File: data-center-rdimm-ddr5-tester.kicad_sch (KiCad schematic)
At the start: 2 parts

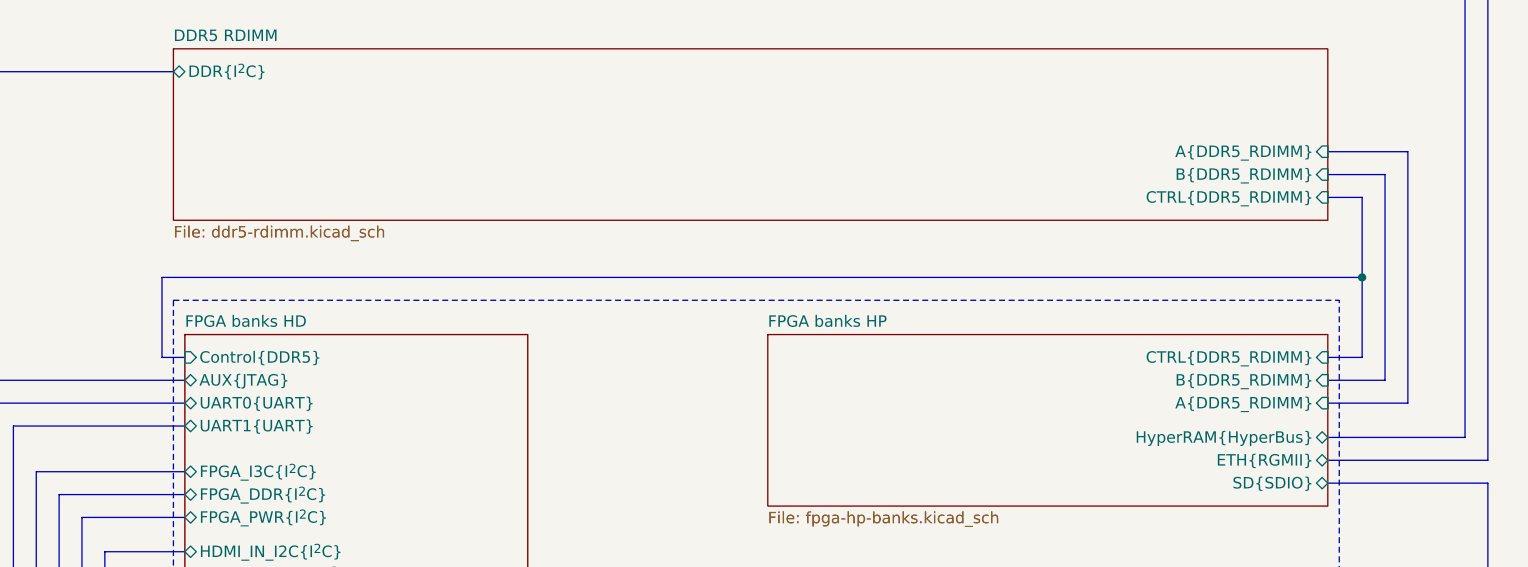
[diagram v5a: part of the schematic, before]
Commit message: [#68016] Solve ERC warrings and errors
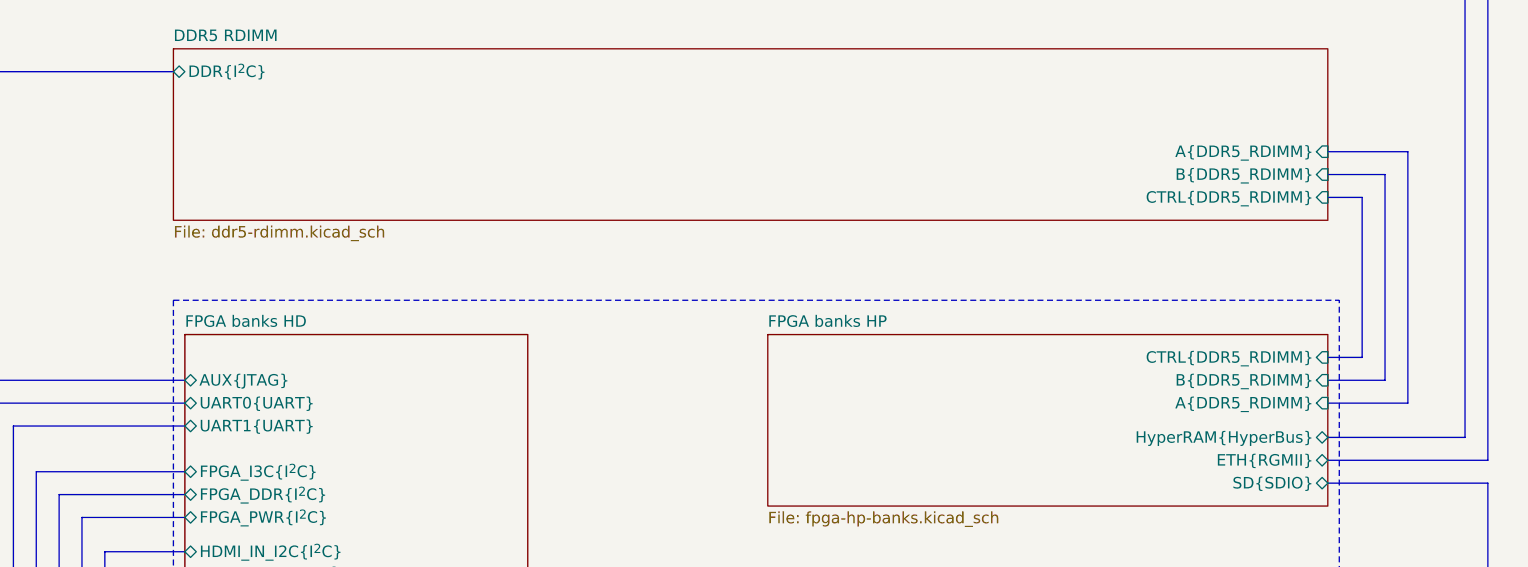
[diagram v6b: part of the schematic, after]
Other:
- sheet FPGA banks HD ports: added none; removed Control{DDR5}
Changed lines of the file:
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@@
     (comment 2 "Antmicro Ltd")
   )
-  (bus_alias "DDR5_RDIMM" (members "DQ[0..31]" "CA[0..6]" "CB[0..7]" "CK_P" "CK_N" "PAR" "DLBDQ" "DLBDQS" "~{ALERT}" "~{RESET}" "DQS0_P" "DQS0_N" "DQS1_P" "DQS1_N" "DQS2_P" "DQS2_N" "DQS3_P" "DQS3_N" "DQS4_P" "DQS4_N" "DQS5_P" "DQS5_N" "DQS6_P" "DQS6_N" "DQS7_P" "DQS7_N" "DQS8_P" "DQS8_N" "DQS9_P" "DQS9_N" "CS0_c" "CS1_c"))
+  (bus_alias "DDR5_RDIMM" (members "DQ[0..31]" "CA[0..6]" "CB[0..7]" "CK_P" "CK_N" "PAR" "DLBDQ" "DLBDQS" "~{ALERT}" "~{RESET}" "DQS0_P" "DQS0_N" "DQS1_P" "DQS1_N" "DQS2_P" "DQS2_N" "DQS3_P" "DQS3_N" "DQS4_P" "DQS4_N" "DQS5_P" "DQS5_N" "DQS6_P" "DQS6_N" "DQS7_P" "DQS7_N" "DQS8_P" "DQS8_N" "DQS9_P" "DQS9_N" "CS0_c" "CS1_c" "PWR_GOOD"))
   (bus_alias "HyperBus" (members "~{CS}" "CK_P" "CK_N" "RWDS" "DQ[0..7]" "~{RESET}"))
   (bus_alias "I^{2}C" (members "SDA" "SCL"))
@@
   (junction (at 142.24 217.17) (diameter 0) (color 0 0 0 0)
   )
-  (junction (at 276.86 76.2) (diameter 0) (color 0 0 0 0)
-  )
   (junction (at 134.62 195.58) (diameter 0) (color 0 0 0 0)
   )
@@
     (stroke (width 0) (type default))
   )
-  (bus (pts (xy 146.05 85.09) (xy 143.51 85.09))
-    (stroke (width 0) (type default))
-  )
   (bus (pts (xy 134.62 102.87) (xy 134.62 195.58))
     (stroke (width 0) (type default))
@@
   )
   (bus (pts (xy 283.21 157.48) (xy 273.05 157.48))
-    (stroke (width 0) (type default))
-  )
-  (bus (pts (xy 276.86 85.09) (xy 276.86 76.2))
     (stroke (width 0) (type default))
   )
@@
     (stroke (width 0) (type default))
   )
-  (bus (pts (xy 143.51 76.2) (xy 276.86 76.2))
-    (stroke (width 0) (type default))
-  )
-  (bus (pts (xy 276.86 76.2) (xy 276.86 67.31))
+  (bus (pts (xy 276.86 67.31) (xy 276.86 85.09))
     (stroke (width 0) (type default))
   )
@@
   )
   (bus (pts (xy 124.46 90.17) (xy 146.05 90.17))
-    (stroke (width 0) (type default))
-  )
-  (bus (pts (xy 143.51 85.09) (xy 143.51 76.2))
     (stroke (width 0) (type default))
   )
@@
       (effects (font (size 1.27 1.27)) (justify left top))
     )
-    (pin "Control{DDR5}" input (at 146.05 85.09 180)
-      (effects (font (size 1.27 1.27)) (justify left))
-    )
     (pin "FPGA_PWR{I^{2}C}" bidirectional (at 146.05 102.87 180)
